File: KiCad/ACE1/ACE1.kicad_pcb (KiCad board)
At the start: 2 copper layers, 198.2 x 224.4 mm, 148 parts, among them IC1 78T, Q1 2N3904, Q2 2N2369, Q3 BC183, Q4 2N3904, X1 6.556MHz

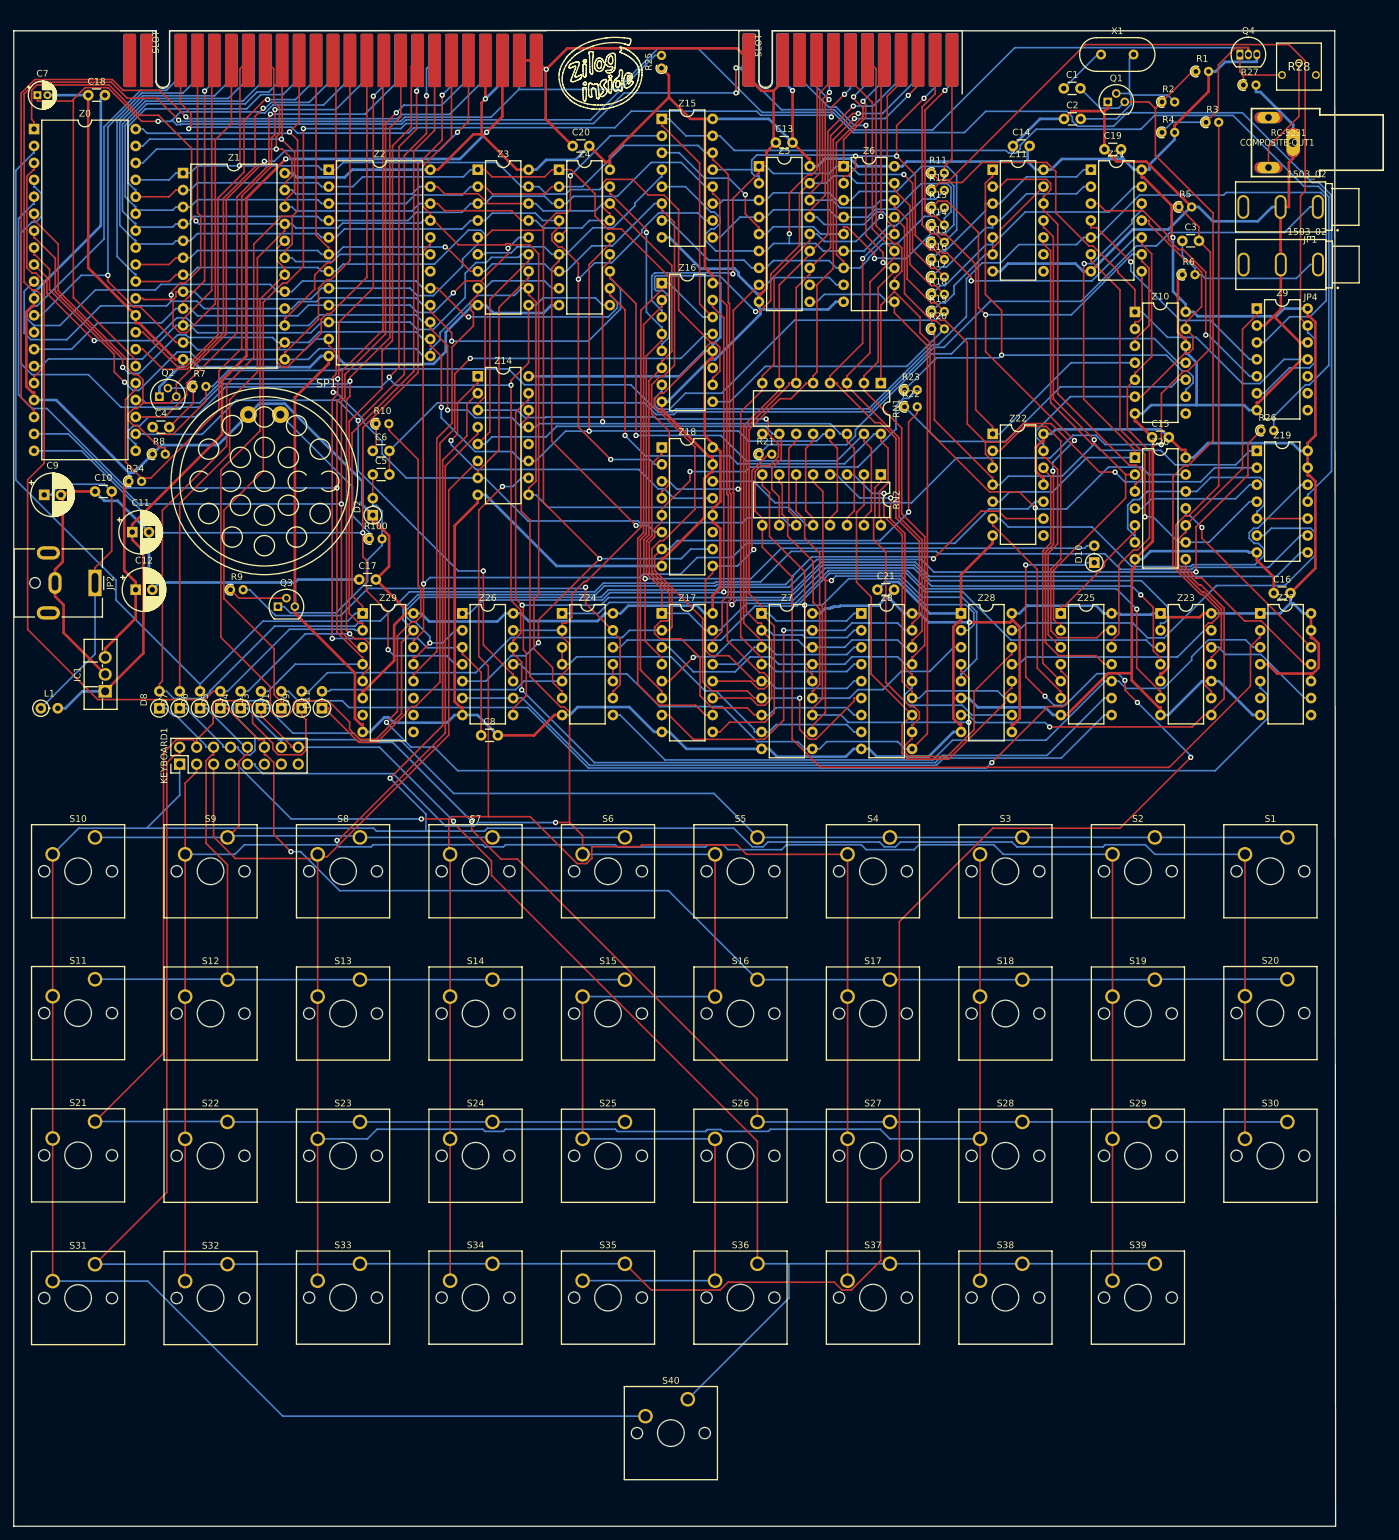
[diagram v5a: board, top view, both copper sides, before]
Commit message: Update IO port decoding.
Signed-off-by: John Bradley <flypie@rocketmail.com>
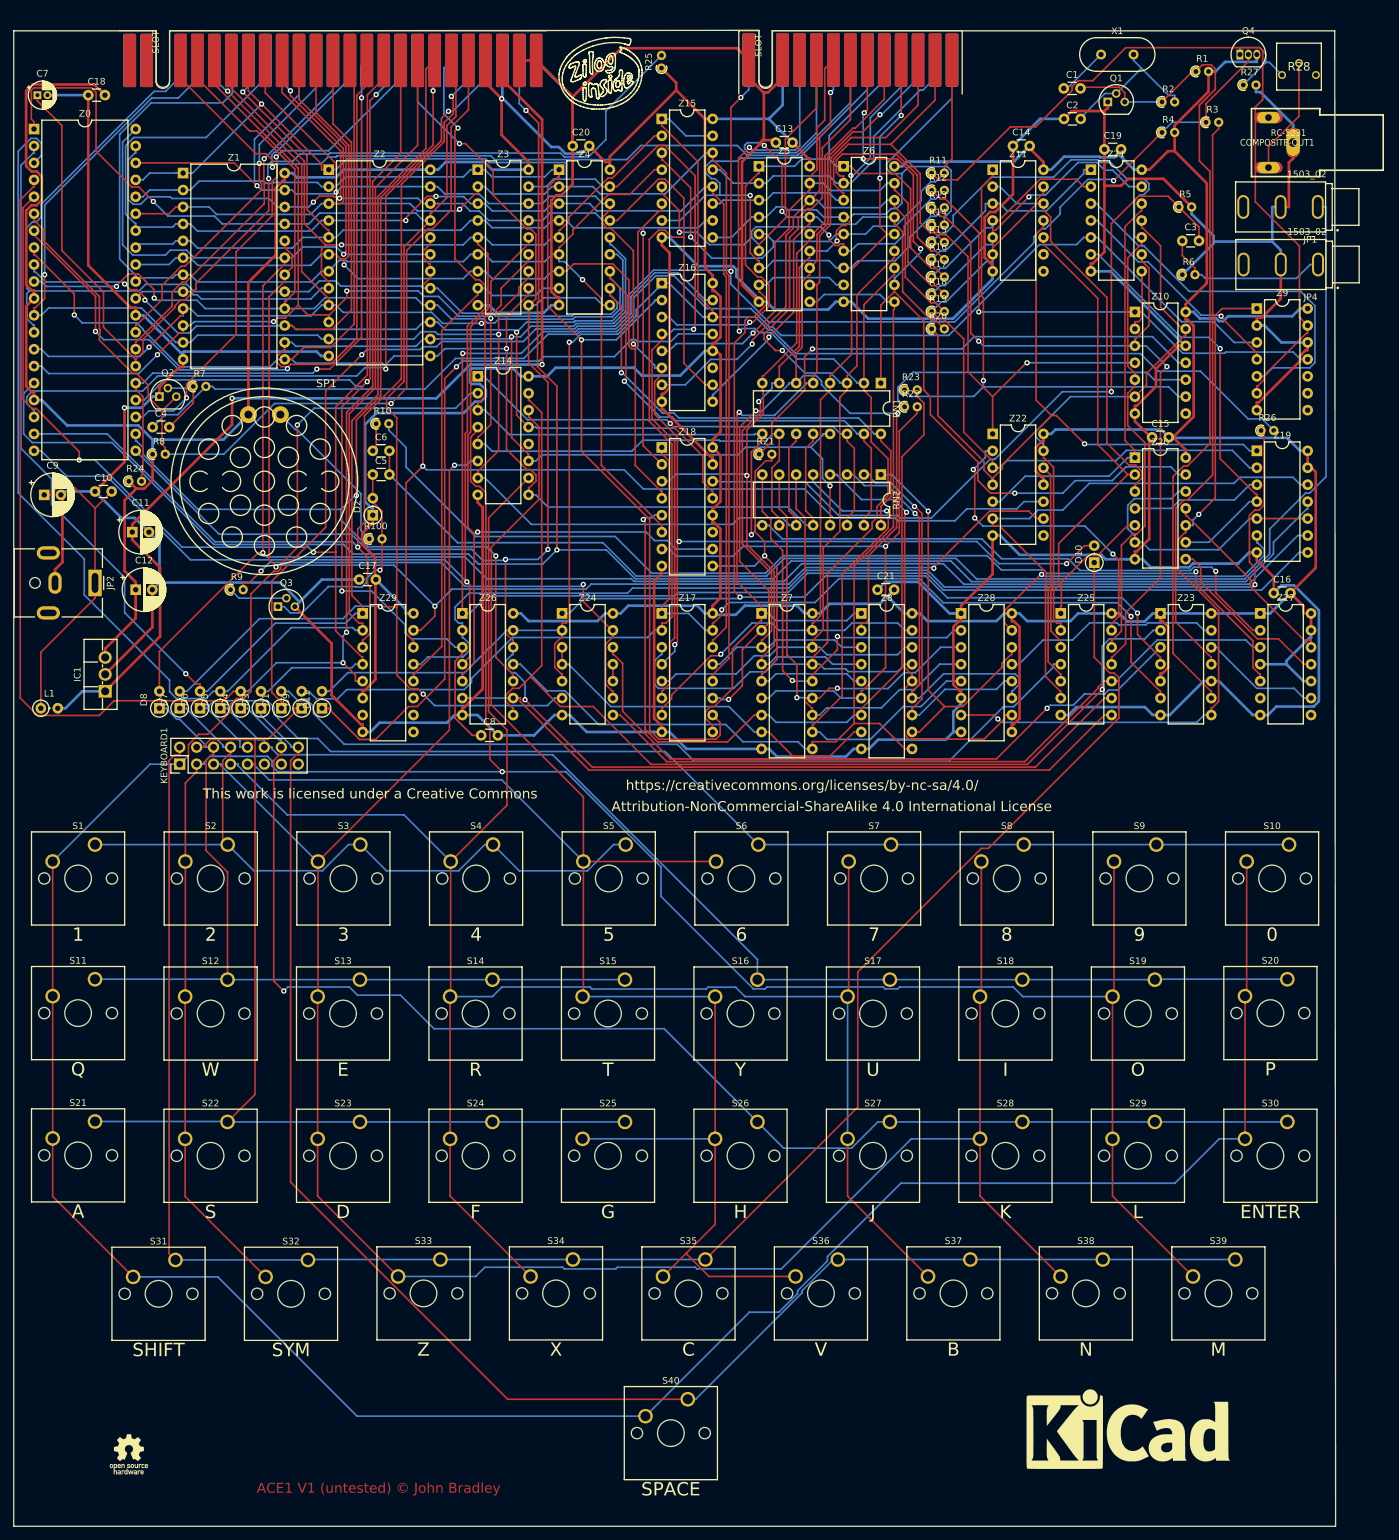
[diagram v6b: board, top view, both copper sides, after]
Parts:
- added REF**: Polarity_Center_Positive_6mm_SilkScreen, Symbol:Polarity_Center_Positive_6mm_SilkScreen, B.Cu at (80.6, 126.4)
- added REF**: KiCad-Logo_12mm_SilkScreen, Symbol:KiCad-Logo_12mm_SilkScreen, F.Cu at (243.8, 253.4)
- added REF**: OSHW-Logo_5.7x6mm_SilkScreen, Symbol:OSHW-Logo_5.7x6mm_SilkScreen, F.Cu at (94.0, 257.2)
- moved S10 179.1 mm to (268.0, 165.7)
- moved S1 178.8 mm to (88.9, 165.7)
- moved S9 139.3 mm to (248.1, 165.7)
- moved S2 139.1 mm to (108.8, 165.7)
- moved S8 99.5 mm to (228.2, 165.7)
- moved S3 99.3 mm to (128.7, 165.7)
- moved S7 59.8 mm to (208.3, 165.7)
- moved S4 59.5 mm to (148.6, 165.7)
- moved S6 20.0 mm to (188.4, 165.7)
- moved S5 19.8 mm to (168.5, 165.7)
- moved S31 12.1 mm to (101.0, 228.0)
- moved S32 12.1 mm to (120.8, 228.0)
- moved S33 12.1 mm to (140.7, 228.0)
- moved S34 12.1 mm to (160.6, 228.0)
- moved S35 12.1 mm to (180.4, 228.0)
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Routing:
- net /ROW8: track 373.3 -> 290.6 mm, vias 5 -> 0
- net /ROW12: track 104.2 -> 182.4 mm
- net VCC: track 836.2 -> 914.3 mm, vias 4 -> 1
- net /ROW11: track 190.8 -> 115.2 mm
- net /COLA: track 472.9 -> 416.4 mm
- net Net-(D11-Pad2): track 302.9 -> 253.4 mm, vias 0 -> 1
- net Net-(C5-Pad2): track 159.4 -> 202.9 mm
- net Net-(Z1-Pad18): track 224.6 -> 181.3 mm, vias 1 -> 3
- net /~VHOLD: track 176.8 -> 217.3 mm
- net /VD6: track 146.7 -> 186.5 mm
- net Net-(R10-Pad2): track 193.8 -> 155.4 mm
- net /CNT0: track 230.2 -> 193.2 mm
- net /VD2: track 137.3 -> 169.6 mm, vias 1 -> 4
- net /DA0: track 325.4 -> 293.4 mm, vias 4 -> 5
- net /ROW15: track 209.3 -> 238.7 mm, vias 1 -> 0
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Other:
- board text added: "7.5 - 9 v"
- board text added: "ACE1 V1 (untested) © John Bradley"
- board text added: "Attribution-NonCommercial-ShareAlike 4.0 International License"
- board text added: "This work is licensed under a Creative Commons"
- board text added: "https://creativecommons.org/licenses/by-nc-sa/4.0/"

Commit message: Fix Main Keyboard Socket
Signed-off-by: John Bradley <flypie@rocketmail.com>
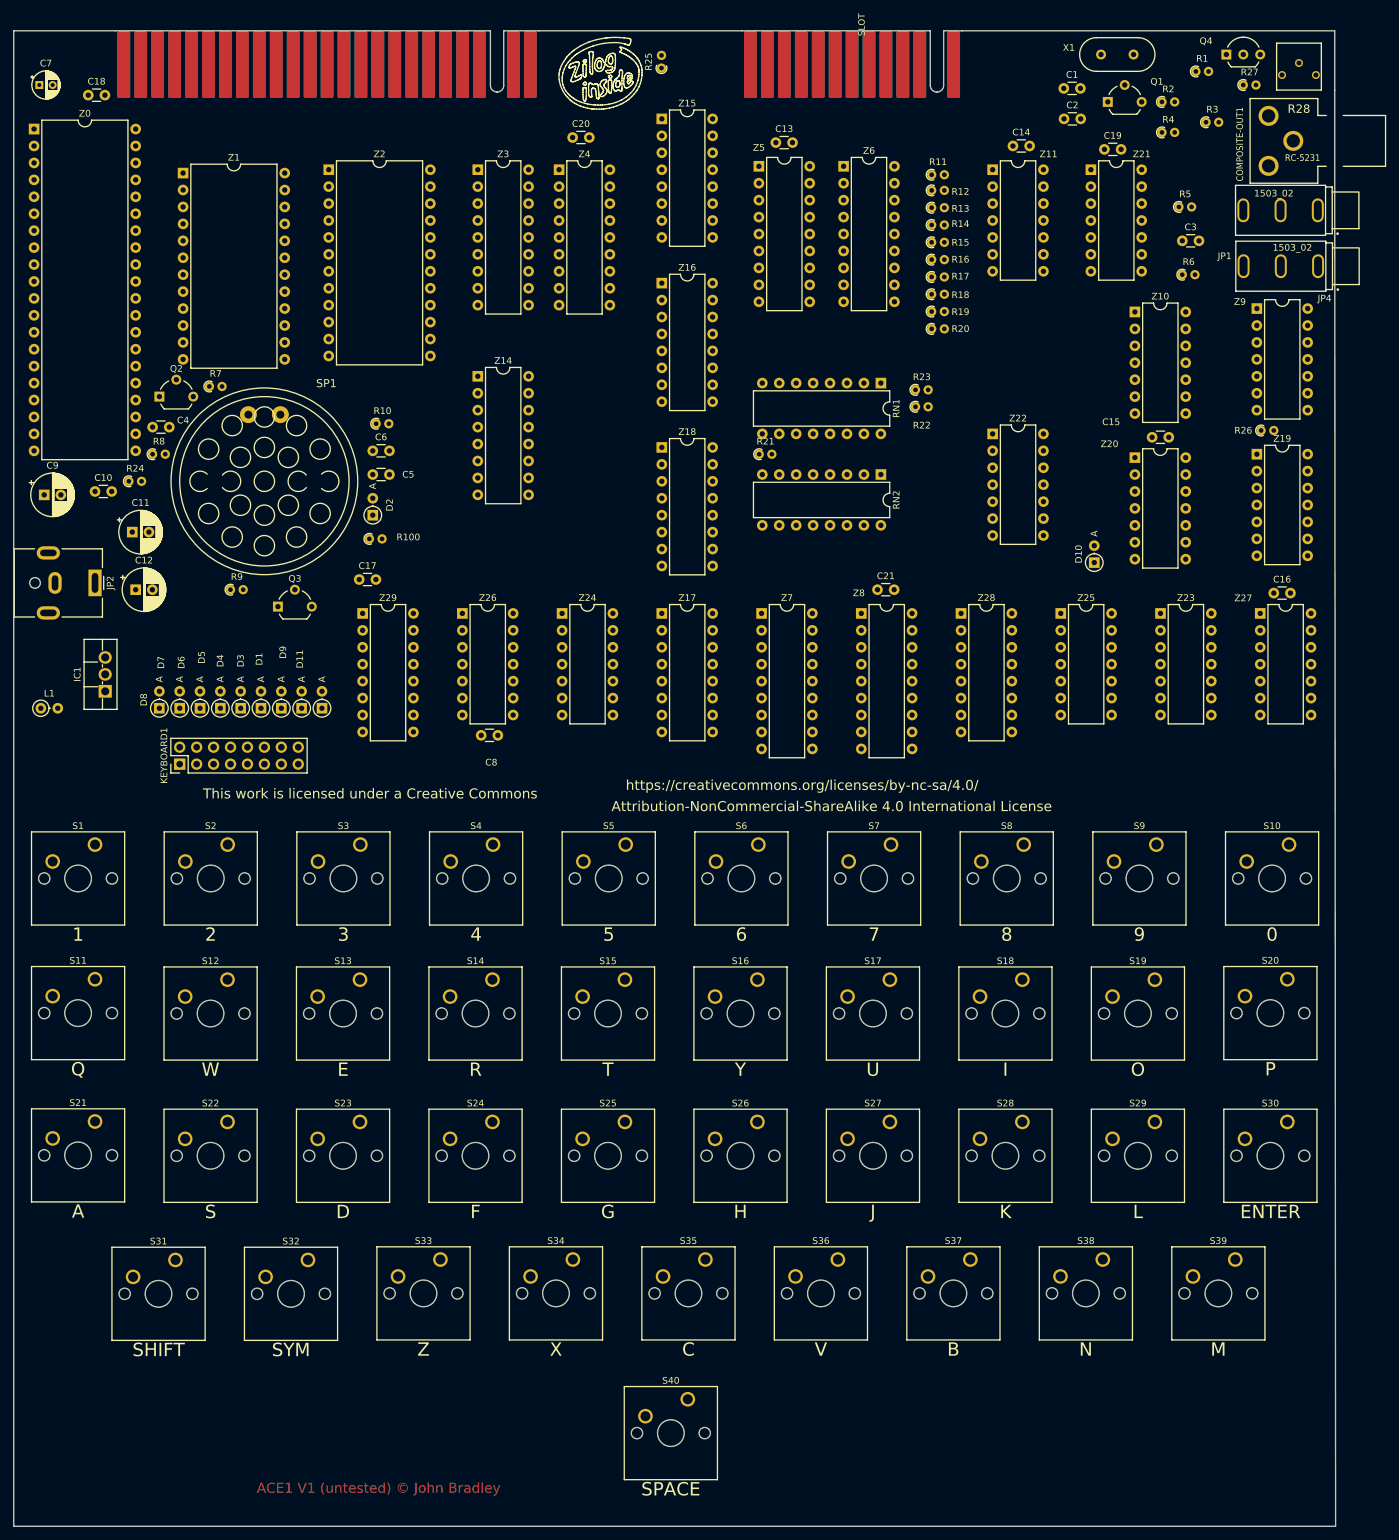
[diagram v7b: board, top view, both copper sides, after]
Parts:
- removed REF**: Polarity_Center_Positive_6mm_SilkScreen, Symbol:Polarity_Center_Positive_6mm_SilkScreen
- removed REF**: KiCad-Logo_12mm_SilkScreen, Symbol:KiCad-Logo_12mm_SilkScreen
- removed REF**: OSHW-Logo_5.7x6mm_SilkScreen, Symbol:OSHW-Logo_5.7x6mm_SilkScreen
- C7: footprint Capacitor_THT:CP_Radial_D4.0mm_P1.50mm -> Capacitor_THT:CP_Radial_D4.0mm_P2.00mm
- Logo1: footprint Symbol:ZilogInsideBack -> ExtraFootprints:ZilogInsideBack
- Logo2: footprint Symbol:ZilogInsideFront -> ExtraFootprints:ZilogInsideFront
- Q1, Q2, Q3: footprint Package_TO_SOT_THT:TO-92 -> Package_TO_SOT_THT:TO-92_Wide
- Q4: footprint Package_TO_SOT_THT:TO-92_Inline -> Package_TO_SOT_THT:TO-92_Inline_Wide
- R28: footprint SamacSys_Parts:3362H1103LF -> ExtraFootprints:3362H1103LF
- moved E1 28.7 mm to (155.4, 43.7)
- moved E2 15.8 mm to (218.9, 43.7)
- moved COMPOSITE-OUT1 10.6 mm to (274.8, 66.5)
- moved R7 2.42 mm to (106.0, 97.0)
- moved Q4 2.03 mm to (258.6, 47.2)
- moved R22 1.63 mm to (211.9, 100.1)
- moved R23 1.63 mm to (211.9, 97.5)
- moved C7 1.55 mm to (80.5, 51.8)
- moved C20 1.27 mm to (160.5, 59.7)
- moved JP1 0.51 mm to (266.7, 70.6)
- moved Z19 0.50 mm to (263.1, 107.2)
- moved JP4 0.25 mm to (266.7, 79.0)
- moved R11 0.25 mm to (214.4, 65.3)
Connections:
- net /~CLK renamed /~{CLK}
- net /~VHOLD renamed /~{VHOLD}
- C7 pad 1: /~RESET -> /~{RESET}
- C8 pad 1: /~WAIT -> /~{WAIT}
- COMPOSITE-OUT1 pad 3: Net-(COMPOSITE-OUT1-Pad3) -> unconnected-(COMPOSITE-OUT1-SHUNT-Pad3)
- E1 pad N.C.1: Net-(E1-PadN.C.1) -> unconnected-(E1-NC.1-PadN.C.1)
- E1 pad N.C.2: Net-(E1-PadN.C.2) -> unconnected-(E1-NC.2-PadN.C.2)
- E1 pad N.C.3: Net-(E1-PadN.C.3) -> unconnected-(E1-NC.3-PadN.C.3)
- E1 pad N.C.4: Net-(E1-PadN.C.4) -> unconnected-(E1-NC.4-PadN.C.4)
- E2 pad N.C.: Net-(E2-PadN.C.) -> unconnected-(E2-NC.1-PadN.C.)
- E2 pad WE: /~WE -> /~{WE}
- JP1 pad 3: Net-(JP1-Pad3) -> unconnected-(JP1-Pad3)
- JP4 pad 3: Net-(JP4-Pad3) -> unconnected-(JP4-Pad3)
- KEYBOARD1 pad 1: /COLA -> /ROW8
- KEYBOARD1 pad 10: /ROW12 -> /COLE
- KEYBOARD1 pad 11: Net-(KEYBOARD1-Pad11) -> /ROW13
- KEYBOARD1 pad 12: /ROW13 -> VCC
- KEYBOARD1 pad 13: Net-(KEYBOARD1-Pad13) -> /ROW14
- KEYBOARD1 pad 14: /ROW14 -> /~{RESET}
- KEYBOARD1 pad 15: Net-(KEYBOARD1-Pad15) -> /ROW15
- KEYBOARD1 pad 16: /ROW15 -> GND
- KEYBOARD1 pad 2: /ROW8 -> /COLA
- KEYBOARD1 pad 3: /COLB -> /ROW9
- KEYBOARD1 pad 4: /ROW9 -> /COLB
- KEYBOARD1 pad 5: /COLC -> /ROW10
- KEYBOARD1 pad 6: /ROW10 -> /COLC
- KEYBOARD1 pad 7: /COLD -> /ROW11
- KEYBOARD1 pad 8: /ROW11 -> /COLD
- KEYBOARD1 pad 9: /COLE -> /ROW12
- R24 pad 2: /~BUSRQ -> /~{BUSRQ}
- R25 pad 2: /~RESET -> /~{RESET}
- R28 pad 3: Net-(R28-Pad3) -> unconnected-(R28-Pad3)
- Z0 pad 16: /~INT -> /~{INT}
- Z0 pad 18: /~HALT -> /~{HALT}
- Z0 pad 19: /~MREQ -> /~{MREQ}
- Z0 pad 20: /~IOREQ -> /~{IOREQ}
- Z0 pad 21: /~WR -> /~{WR}
- Z0 pad 22: /~RD -> /~{RD}
- Z0 pad 23: /~BUSAK -> /~{BUSAK}
- Z0 pad 24: /~WAIT -> /~{WAIT}
- Z0 pad 25: /~BUSRQ -> /~{BUSRQ}
- Z0 pad 26: /~RESET -> /~{RESET}
- Z0 pad 27: /~M1 -> /~{M1}
- Z0 pad 28: /~REFSH -> /~{REFSH}
- Z10 pad 8: Net-(Z10-Pad8) -> unconnected-(Z10B-Q3-Pad8)
- Z11 pad 8: Net-(Z11-Pad8) -> unconnected-(Z11B-Q3-Pad8)
- Z11 pad 9: Net-(Z11-Pad9) -> unconnected-(Z11B-Q2-Pad9)
- Z14 pad 12: Net-(Z14-Pad12) -> unconnected-(Z14-I5-Pad12)
- Z16 pad 11: Net-(Z16-Pad11) -> unconnected-(Z16-O5b-Pad11)
- Z18 pad 11: Net-(Z18-Pad11) -> unconnected-(Z18-O5b-Pad11)
- Z19 pad 11: /~INT -> /~{INT}
- Z19 pad 4: Net-(Z19-Pad4) -> /VIDEN
- Z19 pad 5: /VIDEN -> Net-(Z19-Pad5)
- Z20 pad 12: /VIDEN -> Net-(Z19-Pad5)
- Z20 pad 6: /VIDEN -> Net-(Z19-Pad5)
- Z20 pad 9: Net-(Z19-Pad4) -> /VIDEN
- Z21 pad 6: Net-(Z19-Pad4) -> /VIDEN
- Z25 pad 9: /~WR -> /~{WR}
- Z26 pad 10: /~RD -> /~{RD}
- Z26 pad 12: /~WR -> /~{WR}
- Z26 pad 3: /~WAIT -> /~{WAIT}
- Z26 pad 4: /~IOREQ -> /~{IOREQ}
- Z27 pad 6: Net-(Z27-Pad6) -> unconnected-(Z27A-~{Q}-Pad6)
- Z27 pad 8: Net-(Z27-Pad8) -> unconnected-(Z27B-~{Q}-Pad8)
- Z29 pad 10: Net-(Z29-Pad10) -> unconnected-(Z29-O5-Pad10)
- Z29 pad 11: Net-(Z29-Pad11) -> unconnected-(Z29-O4-Pad11)
- Z29 pad 3: /~MREQ -> /~{MREQ}
- Z29 pad 7: Net-(Z29-Pad7) -> unconnected-(Z29-O7-Pad7)
- Z29 pad 9: Net-(Z29-Pad9) -> unconnected-(Z29-O6-Pad9)
- Z3 pad 10: /~WR -> /~{WR}
- Z4 pad 10: /~WR -> /~{WR}
- Z9 pad 10: Net-(Z9-Pad10) -> unconnected-(Z9B-Q1-Pad10)
- Z9 pad 8: Net-(Z9-Pad8) -> unconnected-(Z9B-Q3-Pad8)
- Z9 pad 9: Net-(Z9-Pad9) -> unconnected-(Z9B-Q2-Pad9)
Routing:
- net GND: track 1012.5 -> 0.00 mm, vias 1 -> 0
- net VCC: track 914.3 -> 0.00 mm, vias 1 -> 0
- net /COLA: track 416.4 -> 0.00 mm, vias 1 -> 0
- net /COLB: track 360.8 -> 0.00 mm, vias 1 -> 0
- net /AD10: track 336.2 -> 0.00 mm, vias 2 -> 0
- net /COLC: track 324.3 -> 0.00 mm, vias 1 -> 0
- net /COLD: track 299.4 -> 0.00 mm
- net /~INT: track 296.5 -> 0.00 mm, vias 2 -> 0
- net /DA0: track 293.4 -> 0.00 mm, vias 5 -> 0
- net /ROW8: track 290.6 -> 0.00 mm
- net /~WR: track 285.9 -> 0.00 mm, vias 4 -> 0
- net /AD9: track 281.2 -> 0.00 mm, vias 2 -> 0
- net /COLE: track 276.6 -> 0.00 mm
- net /VIDEO: track 256.4 -> 0.00 mm, vias 4 -> 0
- net /DA4: track 255.7 -> 0.00 mm, vias 4 -> 0
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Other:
- board size 198.2 x 224.4 mm -> 198.2 x 224.3 mm
- net class Default removed
- net class POWER removed
